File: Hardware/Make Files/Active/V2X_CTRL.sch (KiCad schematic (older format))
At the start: 37 parts, among them CON1 AVR-PDI-6, P20 Jumper 1, P21 Jumper 2, P22 CONN_02X04, P23 Jumper 3, P24 Jumper 4, Q16 2N7000, Q17 2N7000, Q18 2N7000, Q19 2N7000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

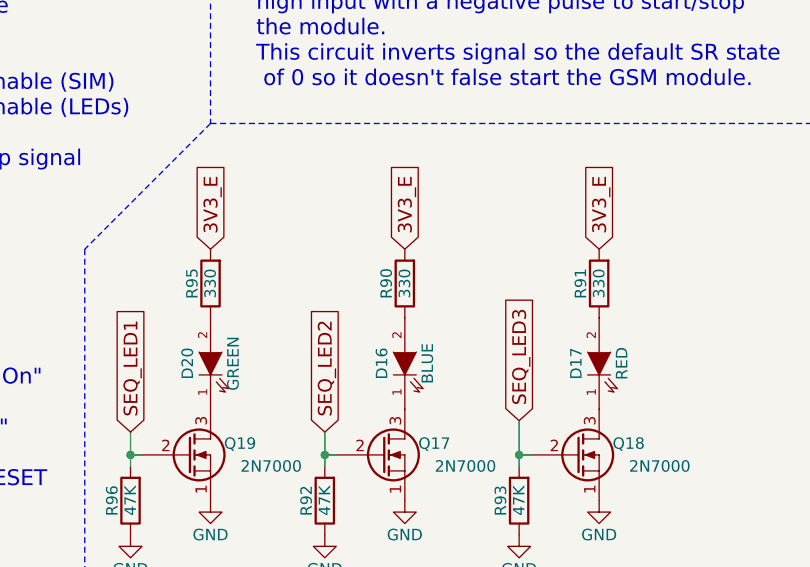
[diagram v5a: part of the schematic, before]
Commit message: Added learnings from V1.2 build
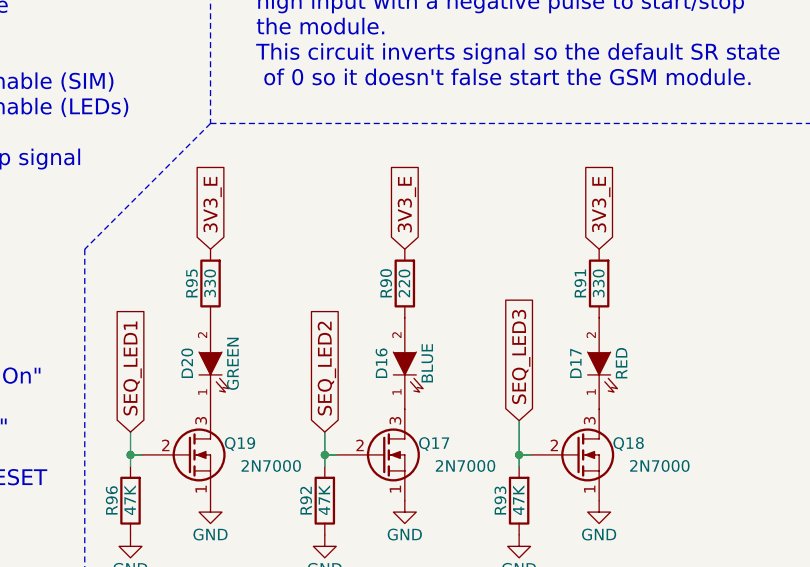
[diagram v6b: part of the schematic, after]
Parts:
- CON1: Mouse PN 571-5-146130-2 -> 855-M20-9980346
- D16: Mouse PN 720-LSR976-NR-1 -> 710-150080BS75000
- D17: Mouse PN 710-150080BS75000 -> 710-150080RS75000
- D20: Mouse PN 720-LSR976-NR-1 -> 710-150080GS75000
- P22: Mouse PN 571-146130-3 -> 855-M20-9980446
- R90: value 330 -> 220; Mouse PN 71-CRCW0603-330-E3 -> 71-CRCW0603-220-E3
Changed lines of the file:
@@
 F 2 "Pin_Headers:Pin_Header_Angled_2x03" V 1130 1985 50  0001 C CNN
 F 3 "http://www.mouser.com/ds/2/418/NG_CD_146130_L_146130_c.dwg-614944.pdf" H 1575 1950 60  0001 C CNN
-F 4 "571-5-146130-2" H 1575 1950 60  0001 C CNN "Mouse PN"
+F 4 "855-M20-9980346" H 1575 1950 60  0001 C CNN "Mouse PN"
 	1    1575 1950
 	1    0    0    -1
@@
 F 1 "BLUE" H 5850 6650 50  0000 C CNN
 F 2 "LEDs:LED-0805" H 5850 6750 60  0001 C CNN
-F 3 "http://www.mouser.com/ds/2/311/LS%20R976%20-%20CHIPLED%200805-318756.pdf" H 5850 6750 60  0001 C CNN
-F 4 "720-LSR976-NR-1" H 5850 6750 60  0001 C CNN "Mouse PN"
+F 3 "http://www.mouser.com/ds/2/239/Lite-On-LTST-C170TBKT-190169.pdf" H 5850 6750 60  0001 C CNN
+F 4 "710-150080BS75000" H 5850 6750 60  0001 C CNN "Mouse PN"
 	1    5850 6750
 	0    -1   -1   0
@@
 F 1 "RED" H 6700 6650 50  0000 C CNN
 F 2 "LEDs:LED-0805" H 6700 6750 60  0001 C CNN
-F 3 "http://www.mouser.com/ds/2/445/150080BS75000-368924.pdf" H 6700 6750 60  0001 C CNN
-F 4 "710-150080BS75000" H 6700 6750 60  0001 C CNN "Mouse PN"
+F 3 "http://www.mouser.com/ds/2/445/150080RS75000-368622.pdf" H 6700 6750 60  0001 C CNN
+F 4 "710-150080RS75000" H 6700 6750 60  0001 C CNN "Mouse PN"
 	1    6700 6750
 	0    -1   -1   0
@@
 F 2 "Pin_Headers:Pin_Header_Straight_2x04" H 9000 3000 60  0001 C CNN
 F 3 "http://www.mouser.com/ds/2/418/NG_CD_146130_L_146130_c.dwg-684736.pdf" H 9000 3000 60  0001 C CNN
-F 4 "571-146130-3" H 9000 4200 60  0001 C CNN "Mouse PN"
+F 4 "855-M20-9980446" H 9000 4200 60  0001 C CNN "Mouse PN"
 	1    9000 4200
 	1    0    0    -1
@@
 P 5850 6400
 F 0 "R90" V 5930 6400 50  0000 C CNN
-F 1 "330" V 5850 6400 50  0000 C CNN
+F 1 "220" V 5850 6400 50  0000 C CNN
 F 2 "Custom Parts:R_0603_sm" V 5780 6400 30  0001 C CNN
 F 3 "http://www.mouser.com/ds/2/427/dcrcwe3-109170.pdf" H 5850 6400 30  0001 C CNN
-F 4 "71-CRCW0603-330-E3" H 5850 6400 60  0001 C CNN "Mouse PN"
+F 4 "71-CRCW0603-220-E3" H 5850 6400 60  0001 C CNN "Mouse PN"
 	1    5850 6400
 	-1   0    0    1
@@
 F 1 "GREEN" H 5000 6650 50  0000 C CNN
 F 2 "LEDs:LED-0805" H 5000 6750 60  0001 C CNN
-F 3 "http://www.mouser.com/ds/2/311/LS%20R976%20-%20CHIPLED%200805-318756.pdf" H 5000 6750 60  0001 C CNN
-F 4 "720-LSR976-NR-1" H 5000 6750 60  0001 C CNN "Mouse PN"
+F 3 "http://www.mouser.com/ds/2/445/150080GS75000-368928.pdf" H 5000 6750 60  0001 C CNN
+F 4 "710-150080GS75000" H 5000 6750 60  0001 C CNN "Mouse PN"
 	1    5000 6750
 	0    -1   -1   0

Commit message: V2X Build learnings
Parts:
- Q16, Q17, Q18, Q19: symbol Q_NMOS_SGD -> Q_NMOS_GSD
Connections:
- net GND: now also Q16.2 (S), Q17.2 (S), Q18.2 (S), Q19.2 (S); no longer Q16.1 (S), Q17.1 (S), Q18.1 (S), Q19.1 (S)
- net SEQ_LED1: now also Q19.1 (G); no longer Q19.2 (G)
- net SEQ_LED2: now also Q17.1 (G); no longer Q17.2 (G)
- net SEQ_LED3: now also Q18.1 (G); no longer Q18.2 (G)
- net SIM_PWR_ON: now also Q16.1 (G); no longer Q16.2 (G)
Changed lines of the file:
@@
 Connection ~ 6350 7150
 $Comp
-L Q_NMOS_SGD Q16
+L Q_NMOS_GSD Q16
 U 1 1 55FE0BA7
 P 6300 4650
@@
 $EndComp
 $Comp
-L Q_NMOS_SGD Q18
+L Q_NMOS_GSD Q18
 U 1 1 5605B808
 P 6600 7150
@@
 $EndComp
 $Comp
-L Q_NMOS_SGD Q17
+L Q_NMOS_GSD Q17
 U 1 1 5605B89E
 P 5750 7150
@@
 Connection ~ 4650 7150
 $Comp
-L Q_NMOS_SGD Q19
+L Q_NMOS_GSD Q19
 U 1 1 560D95D1
 P 4900 7150
